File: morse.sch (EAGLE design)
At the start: 3 parts, among them IC1 TINY13-20PU

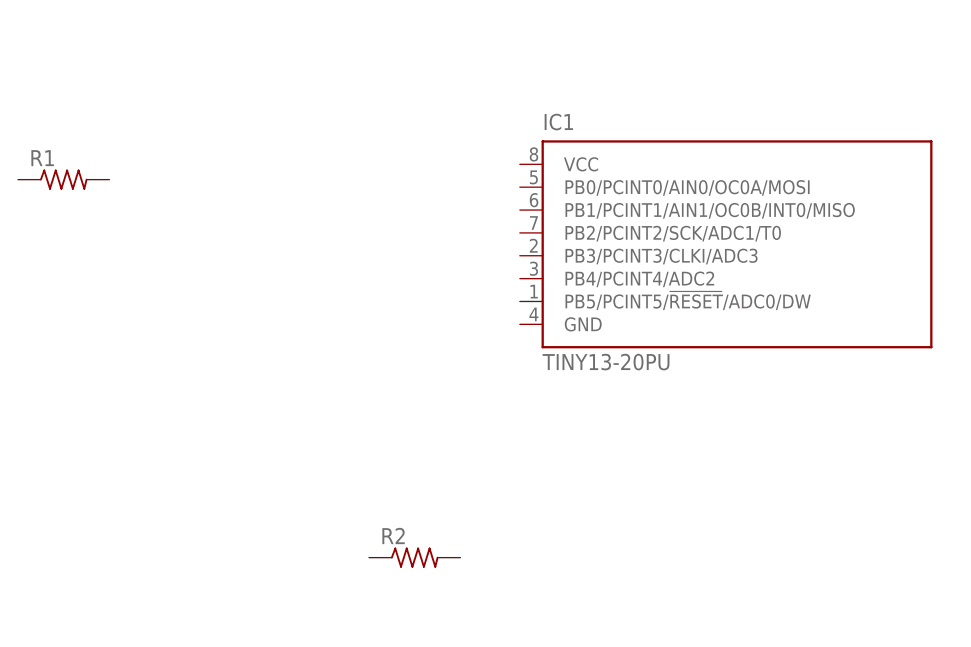
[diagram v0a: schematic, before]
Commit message: replaced schematic diagram
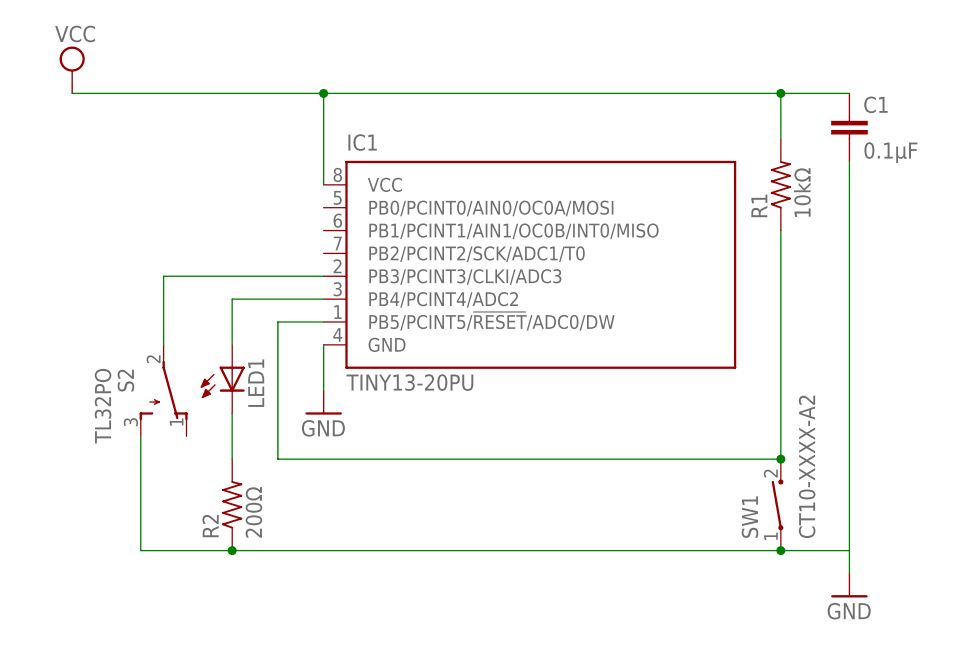
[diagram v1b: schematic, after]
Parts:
- added C1: 0.1μF, capacitor-wima:C2,5-3
- added LED1: (no value), eagle-ltspice:LED_ELD260
- added S2: TL32PO, switch:TL32PO
- added SW1: CT10-XXXX-A2, switch-coto:CT10-XXXX-A2
- R1: value (none) -> 10kΩ; device resistor:R-US_0204/2V -> rcl:R-US_0204/7
- R2: value (none) -> 200Ω; device resistor:R-US_0204/2V -> rcl:R-US_0204/7
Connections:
- new net GND: C1.2, IC1.GND, R2.1, S2.S, SW1.1
- new net N$1: IC1.PB5/PCINT5/!RESET!/ADC0/DW, R1.1, SW1.2
- new net N$2: IC1.PB4/PCINT4/ADC2, LED1.A
- new net N$3: LED1.C, R2.2
- new net N$4: IC1.PB3/PCINT3/CLKI/ADC3, S2.P
- new net VCC: C1.1, IC1.VCC, R1.2
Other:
- moved on the sheet: IC1, R1, R2
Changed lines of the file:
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@@
 <setting verticaltext="up"/>
 </settings>
-<grid distance="1" unitdist="mm" unit="mm" style="lines" multiple="1" display="no" altdistance="0.01" altunitdist="inch" altunit="inch"/>
+<grid distance="0.1" unitdist="inch" unit="inch" style="dots" multiple="1" display="yes" altdistance="0.01" altunitdist="inch" altunit="inch"/>
 <layers>
 <layer number="1" name="Top" color="4" fill="1" visible="no" active="no"/>
@@
 <layer number="97" name="Info" color="7" fill="1" visible="yes" active="yes"/>
 <layer number="98" name="Guide" color="6" fill="1" visible="yes" active="yes"/>
+<layer number="99" name="SpiceOrder" color="5" fill="1" visible="yes" active="yes"/>
 </layers>
 <schematic xreflabel="%F%N/%S.%C%R" xrefpart="/%S.%C%R">
@@
 </classes>
 <parts>
+<part name="R1" library="rcl" deviceset="R-US_" device="0204/7" value="10kΩ"/>
+<part name="R2" library="rcl" deviceset="R-US_" device="0204/7" value="200Ω"/>
+<part name="C1" library="capacitor-wima" deviceset="C" device="2,5-3" value="0.1μF"/>
+<part name="LED1" library="eagle-ltspice" deviceset="LED_E" device="LD260"/>
+<part name="SW1" library="switch-coto" deviceset="CT10-XXXX-" device="A2"/>
+<part name="S2" library="switch" deviceset="TL32PO" device=""/>
+<part name="GND1" library="supply1" deviceset="GND" device=""/>
+<part name="GND2" library="supply1" deviceset="GND" device=""/>
+<part name="SUPPLY1" library="supply2" deviceset="VCC" device=""/>
 <part name="IC1" library="atmel" deviceset="TINY13" device="PU" technology="-20"/>
-<part name="R1" library="resistor" deviceset="R-US_" device="0204/2V"/>
-<part name="R2" library="resistor" deviceset="R-US_" device="0204/2V"/>
 </parts>
 <sheets>
@@
 </plain>
 <instances>
-<instance part="IC1" gate="G$1" x="98" y="48"/>
-<instance part="R1" gate="G$1" x="27" y="59"/>
-<instance part="R2" gate="G$1" x="66" y="17"/>
+<instance part="R1" gate="G$1" x="106.68" y="58.42" rot="R90"/>
+<instance part="R2" gate="G$1" x="45.72" y="22.86" rot="R90"/>
+<instance part="C1" gate="G$1" x="114.3" y="66.04"/>
+<instance part="LED1" gate="G$1" x="45.72" y="38.1"/>
+<instance part="SW1" gate="G$1" x="106.68" y="22.86" rot="R90"/>
+<instance part="S2" gate="BEF1" x="38.1" y="35.56" rot="R180"/>
+<instance part="GND1" gate="1" x="55.88" y="33.02"/>
+<instance part="GND2" gate="1" x="114.3" y="12.7"/>
+<instance part="SUPPLY1" gate="G$1" x="27.94" y="71.12"/>
+<instance part="IC1" gate="G$1" x="76.2" y="45.72"/>
 </instances>
 <busses>
 </busses>
 <nets>
+<net name="VCC" class="0">
+<segment>
+<pinref part="SUPPLY1" gate="G$1" pin="VCC"/>
+<pinref part="C1" gate="G$1" pin="1"/>
+<wire x1="27.94" y1="68.58" x2="55.88" y2="68.58" width="0.1524" layer="91"/>
+<pinref part="IC1" gate="G$1" pin="VCC"/>
+<wire x1="55.88" y1="68.58" x2="106.68" y2="68.58" width="0.1524" layer="91"/>
+<wire x1="106.68" y1="68.58" x2="114.3" y2="68.58" width="0.1524" layer="91"/>
+<wire x1="55.88" y1="58.42" x2="55.88" y2="68.58" width="0.1524" layer="91"/>
+<pinref part="R1" gate="G$1" pin="2"/>
+<wire x1="106.68" y1="68.58" x2="106.68" y2="63.5" width="0.1524" layer="91"/>
+<junction x="55.88" y="68.58"/>
+<junction x="106.68" y="68.58"/>
+</segment>
+</net>
+<net name="GND" class="0">
+<segment>
+<pinref part="C1" gate="G$1" pin="2"/>
+<pinref part="GND2" gate="1" pin="GND"/>
+<wire x1="114.3" y1="60.96" x2="114.3" y2="17.78" width="0.1524" layer="91"/>
+<wire x1="114.3" y1="17.78" x2="114.3" y2="15.24" width="0.1524" layer="91"/>
+<wire x1="114.3" y1="17.78" x2="106.68" y2="17.78" width="0.1524" layer="91"/>
+<pinref part="S2" gate="BEF1" pin="S"/>
+<wire x1="106.68" y1="17.78" x2="45.72" y2="17.78" width="0.1524" layer="91"/>
+<wire x1="45.72" y1="17.78" x2="35.56" y2="17.78" width="0.1524" layer="91"/>
+<wire x1="35.56" y1="17.78" x2="35.56" y2="30.48" width="0.1524" layer="91"/>
+<pinref part="R2" gate="G$1" pin="1"/>
+<junction x="45.72" y="17.78"/>
+<pinref part="SW1" gate="G$1" pin="1"/>
+<junction x="106.68" y="17.78"/>
+</segment>
+<segment>
+<pinref part="IC1" gate="G$1" pin="GND"/>
+<pinref part="GND1" gate="1" pin="GND"/>
+<wire x1="55.88" y1="40.64" x2="55.88" y2="35.56" width="0.1524" layer="91"/>
+</segment>
+</net>
+<net name="N$1" class="0">
+<segment>
+<pinref part="R1" gate="G$1" pin="1"/>
+<pinref part="SW1" gate="G$1" pin="2"/>
+<wire x1="106.68" y1="53.34" x2="106.68" y2="27.94" width="0.1524" layer="91"/>
+<pinref part="IC1" gate="G$1" pin="PB5/PCINT5/!RESET!/ADC0/DW"/>
+<wire x1="55.88" y1="43.18" x2="50.8" y2="43.18" width="0.1524" layer="91"/>
+<wire x1="50.8" y1="43.18" x2="50.8" y2="27.94" width="0.1524" layer="91"/>
+<wire x1="50.8" y1="27.94" x2="106.68" y2="27.94" width="0.1524" layer="91"/>
+<junction x="106.68" y="27.94"/>
+</segment>
+</net>
+<net name="N$2" class="0">
+<segment>
+<pinref part="IC1" gate="G$1" pin="PB4/PCINT4/ADC2"/>
+<wire x1="55.88" y1="45.72" x2="45.72" y2="45.72" width="0.1524" layer="91"/>
+<pinref part="LED1" gate="G$1" pin="A"/>
+<wire x1="45.72" y1="45.72" x2="45.72" y2="40.64" width="0.1524" layer="91"/>
+</segment>
+</net>
+<net name="N$3" class="0">
+<segment>
+<pinref part="LED1" gate="G$1" pin="C"/>
+<pinref part="R2" gate="G$1" pin="2"/>
+<wire x1="45.72" y1="33.02" x2="45.72" y2="27.94" width="0.1524" layer="91"/>
+</segment>
+</net>
+<net name="N$4" class="0">
+<segment>
+<pinref part="IC1" gate="G$1" pin="PB3/PCINT3/CLKI/ADC3"/>
+<wire x1="55.88" y1="48.26" x2="38.1" y2="48.26" width="0.1524" layer="91"/>
+<pinref part="S2" gate="BEF1" pin="P"/>
+<wire x1="38.1" y1="48.26" x2="38.1" y2="40.64" width="0.1524" layer="91"/>
+</segment>
+</net>
 </nets>
 </sheet>
